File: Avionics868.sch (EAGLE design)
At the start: 65 parts, among them SW1 B3U-1000P-2P-SMD, U1 ATSAMD21G18_QFN, U2 SPX3819M5-L-3-0, U3 MCP73831T-2ACI/OT, U4 MPU-9250, U5 SIM868, U6 BMP180, X1 JSTPH, X2 32.768, X3 ST-USB-001G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

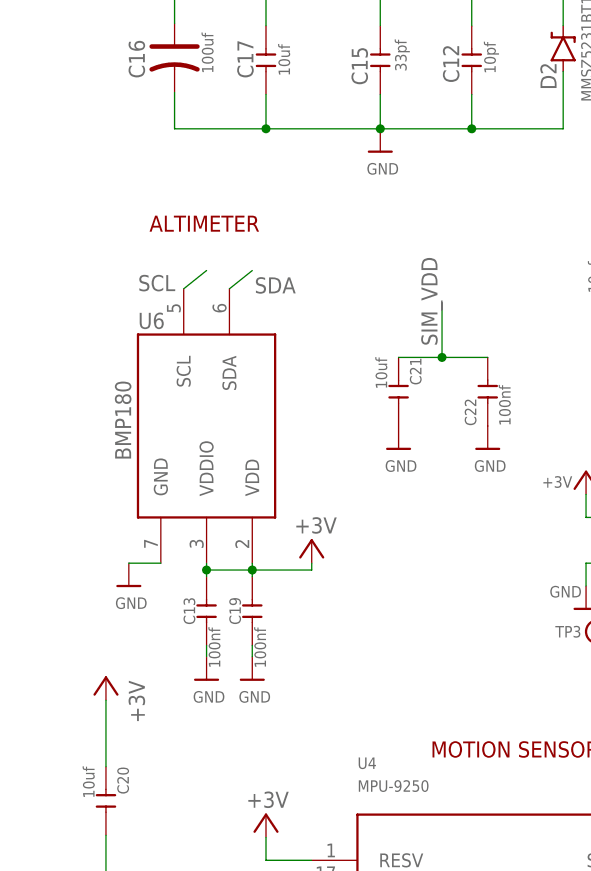
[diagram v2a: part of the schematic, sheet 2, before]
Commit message: Swapped obsolete part BMP180 for BMP280
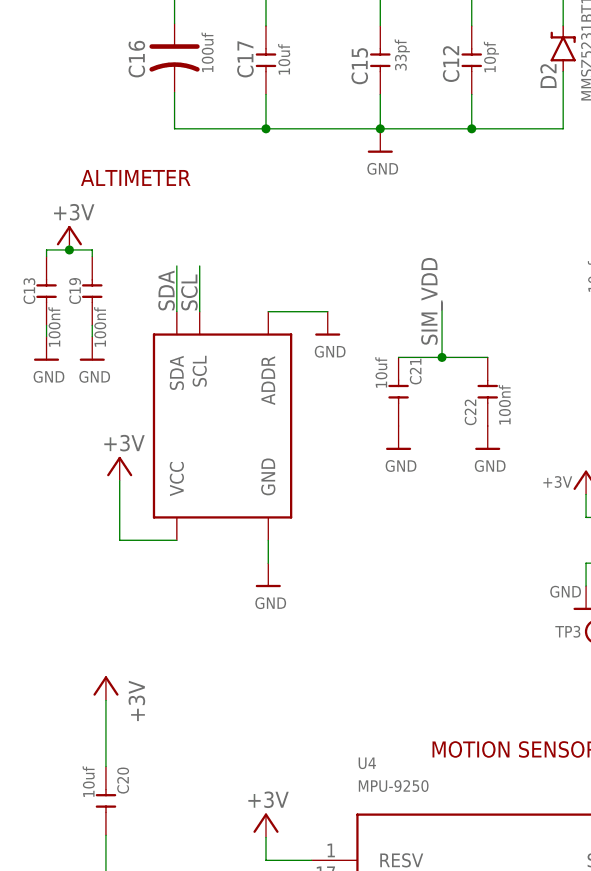
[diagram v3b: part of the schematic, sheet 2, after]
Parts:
- U6: value BMP180 -> BMP280; device SparkFun-Sensors:BMP180 -> BMP280:BMP280
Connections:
- net +3V: now also U6.VCC; no longer U6.VDD, U6.VDDIO
- net GND: now also U6.ADDR
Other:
- moved on the sheet: C13, C19
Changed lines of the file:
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@@
 <part name="R1" library="Seeed-Resistor-2016" deviceset="SMD-RES-100K-5%-1/10W(0603)" device="" value="100K 1/10W"/>
 <part name="FRAME2" library="microbuilder" deviceset="FRAME_A4" device=""/>
-<part name="U6" library="SparkFun-Sensors" deviceset="BMP180" device=""/>
 <part name="U4" library="misc" deviceset="MPU-9250" device=""/>
 <part name="C13" library="Seeed-Capacitor-2016" deviceset="CERAMIC-100NF-25V-10%-X7R(0402)" device="" value="100nf"/>
@@
 <part name="U$14" library="microbuilder" deviceset="GND" device=""/>
 <part name="U$15" library="microbuilder" deviceset="GND" device=""/>
-<part name="U$17" library="microbuilder" deviceset="GND" device=""/>
 <part name="U$18" library="microbuilder" deviceset="GND" device=""/>
 <part name="U$23" library="microbuilder" deviceset="GND" device=""/>
@@
 <part name="X3" library="Seeed-Connector -2016" deviceset="MICRO-USB-SMD-B-WITHOUT-POST-W/P(ST-USB-001G)" device="" value="ST-USB-001G"/>
 <part name="GND2" library="supply1" deviceset="GND" device=""/>
+<part name="U6" library="BMP280" deviceset="BMP280" device=""/>
+<part name="U$53" library="microbuilder" deviceset="GND" device=""/>
+<part name="U$54" library="microbuilder" deviceset="GND" device=""/>
+<part name="+3V15" library="Custom" deviceset="+3V" device=""/>
 </parts>
 <sheets>
@@
 <sheet>
 <plain>
-<text x="20.066" y="128.27" size="1.778" layer="94">ALTIMETER</text>
+<text x="12.446" y="133.35" size="1.778" layer="94">ALTIMETER</text>
 <text x="51.308" y="69.85" size="1.778" layer="94">MOTION SENSOR</text>
 <text x="91.44" y="129.54" size="1.778" layer="94">MICROSD / NANOSIM</text>
@@
 <instances>
 <instance part="FRAME2" gate="G$1" x="0" y="0"/>
-<instance part="U6" gate="G$1" x="26.416" y="106.68" smashed="yes" rot="R270">
-<attribute name="NAME" x="18.796" y="117.475" size="1.778" layer="95"/>
-<attribute name="VALUE" x="16.256" y="111.76" size="1.778" layer="96" rot="R270"/>
-</instance>
 <instance part="U4" gate="G$1" x="60.96" y="43.18"/>
-<instance part="C13" gate="G$1" x="26.416" y="86.106" smashed="yes" rot="R90">
-<attribute name="NAME" x="25.146" y="84.582" size="1.27" layer="95" ratio="10" rot="R90"/>
-<attribute name="VALUE" x="27.94" y="79.756" size="1.27" layer="96" ratio="10" rot="R90"/>
+<instance part="C13" gate="G$1" x="8.636" y="121.666" smashed="yes" rot="R90">
+<attribute name="NAME" x="7.366" y="120.142" size="1.27" layer="95" ratio="10" rot="R90"/>
+<attribute name="VALUE" x="10.16" y="115.316" size="1.27" layer="96" ratio="10" rot="R90"/>
 </instance>
 <instance part="C9" gate="G$1" x="97.79" y="30.48" rot="R180"/>
@@
 <instance part="U5" gate="G$1" x="198.12" y="68.58"/>
 <instance part="U$14" gate="G$1" x="45.72" y="137.16"/>
-<instance part="U$15" gate="G$1" x="26.416" y="78.486"/>
-<instance part="U$17" gate="G$1" x="17.78" y="88.9"/>
+<instance part="U$15" gate="G$1" x="8.636" y="114.046"/>
 <instance part="U$18" gate="G$1" x="104.14" y="27.94"/>
 <instance part="U$23" gate="G$1" x="88.9" y="40.64"/>
@@
 <instance part="U$26" gate="G$1" x="15.24" y="40.64"/>
 <instance part="U$37" gate="G$1" x="147.32" y="116.84"/>
-<instance part="+3V7" gate="G$1" x="38.1" y="93.98" smashed="yes" rot="MR0">
-<attribute name="VALUE" x="40.894" y="94.742" size="1.778" layer="96" rot="MR0"/>
+<instance part="+3V7" gate="G$1" x="11.176" y="128.778" smashed="yes" rot="MR0">
+<attribute name="VALUE" x="13.97" y="129.54" size="1.778" layer="96" rot="MR0"/>
 </instance>
 <instance part="+3V8" gate="G$1" x="91.44" y="55.88" smashed="yes" rot="MR0">
@@
 <attribute name="VALUE" x="33.274" y="49.276" size="1.778" layer="96" rot="MR0"/>
 </instance>
-<instance part="C19" gate="G$1" x="31.496" y="86.106" smashed="yes" rot="R90">
-<attribute name="NAME" x="30.226" y="84.582" size="1.27" layer="95" ratio="10" rot="R90"/>
-<attribute name="VALUE" x="33.02" y="79.756" size="1.27" layer="96" ratio="10" rot="R90"/>
-</instance>
-<instance part="U$7" gate="G$1" x="31.496" y="78.486"/>
+<instance part="C19" gate="G$1" x="13.716" y="121.666" smashed="yes" rot="R90">
+<attribute name="NAME" x="12.446" y="120.142" size="1.27" layer="95" ratio="10" rot="R90"/>
+<attribute name="VALUE" x="15.24" y="115.316" size="1.27" layer="96" ratio="10" rot="R90"/>
+</instance>
+<instance part="U$7" gate="G$1" x="13.716" y="114.046"/>
 <instance part="R4" gate="G$1" x="98.552" y="151.13" rot="R90"/>
 <instance part="R5" gate="G$1" x="106.172" y="151.13" rot="R90"/>
@@
 <instance part="U$35" gate="G$1" x="71.374" y="114.808"/>
 <instance part="U$51" gate="G$1" x="81.28" y="114.808"/>
+<instance part="U6" gate="G$1" x="28.194" y="106.68" rot="R90"/>
+<instance part="U$53" gate="G$1" x="39.878" y="116.84"/>
+<instance part="U$54" gate="G$1" x="33.274" y="88.9"/>
+<instance part="+3V15" gate="G$1" x="16.764" y="103.124" smashed="yes" rot="MR0">
+<attribute name="VALUE" x="19.558" y="103.886" size="1.778" layer="96" rot="MR0"/>
+</instance>
 </instances>
 <busses>
@@
 <net name="GND" class="0">
 <segment>
-<pinref part="U6" gate="G$1" pin="GND"/>
-<wire x1="17.78" y1="91.44" x2="21.336" y2="91.44" width="0.1524" layer="91"/>
-<pinref part="U$17" gate="G$1" pin="GND"/>
-</segment>
-<segment>
 <pinref part="U$15" gate="G$1" pin="GND"/>
 <pinref part="C13" gate="G$1" pin="1"/>
-<wire x1="26.416" y1="81.026" x2="26.416" y2="82.296" width="0.1524" layer="91"/>
+<wire x1="8.636" y1="116.586" x2="8.636" y2="117.856" width="0.1524" layer="91"/>
 </segment>
 <segment>
@@
 <pinref part="U$7" gate="G$1" pin="GND"/>
 <pinref part="C19" gate="G$1" pin="1"/>
-<wire x1="31.496" y1="81.026" x2="31.496" y2="82.296" width="0.1524" layer="91"/>
+<wire x1="13.716" y1="116.586" x2="13.716" y2="117.856" width="0.1524" layer="91"/>
 </segment>
 <segment>
@@
 <pinref part="U$51" gate="G$1" pin="GND"/>
 </segment>
+<segment>
+<pinref part="U6" gate="G$1" pin="ADDR"/>
+<wire x1="33.274" y1="119.38" x2="39.878" y2="119.38" width="0.1524" layer="91"/>
+<pinref part="U$53" gate="G$1" pin="GND"/>
+</segment>
+<segment>
+<pinref part="U6" gate="G$1" pin="GND"/>
+<pinref part="U$54" gate="G$1" pin="GND"/>
+<wire x1="33.274" y1="91.44" x2="33.274" y2="93.98" width="0.1524" layer="91"/>
+</segment>
 </net>
 <net name="SCL" class="0">
-<segment>
-<pinref part="U6" gate="G$1" pin="SCL"/>
-<wire x1="23.876" y1="121.92" x2="26.416" y2="123.952" width="0.1524" layer="91"/>
-<label x="18.796" y="121.666" size="1.778" layer="95"/>
-</segment>
 <segment>
 <pinref part="U4" gate="G$1" pin="SCL/SCLK"/>
@@
 <pinref part="R4" gate="G$1" pin="1"/>
 </segment>
+<segment>
+<pinref part="U6" gate="G$1" pin="SCL"/>
+<wire x1="25.654" y1="119.38" x2="25.654" y2="124.46" width="0.1524" layer="91"/>
+<label x="25.4" y="119.38" size="1.778" layer="95" rot="R90"/>
+</segment>
 </net>
 <net name="SDA" class="0">
-<segment>
-<pinref part="U6" gate="G$1" pin="SDA"/>
-<wire x1="28.956" y1="121.92" x2="31.496" y2="123.952" width="0.1524" layer="91"/>
-<label x="31.75" y="121.412" size="1.778" layer="95"/>
-</segment>
 <segment>
 <pinref part="U4" gate="G$1" pin="SDA/SDI"/>
@@
 <label x="103.632" y="143.51" size="1.778" layer="95"/>
 <pinref part="R5" gate="G$1" pin="1"/>
+</segment>
+<segment>
+<pinref part="U6" gate="G$1" pin="SDA"/>
+<wire x1="23.114" y1="119.38" x2="23.114" y2="124.46" width="0.1524" layer="91"/>
+<label x="22.86" y="119.38" size="1.778" layer="95" rot="R90"/>
 </segment>
 </net>
@@
 <segment>
 <pinref part="C13" gate="G$1" pin="2"/>
-<wire x1="26.416" y1="91.44" x2="26.416" y2="90.678" width="0.1524" layer="91"/>
 <pinref part="C19" gate="G$1" pin="2"/>
-<wire x1="26.416" y1="90.678" x2="26.416" y2="89.916" width="0.1524" layer="91"/>
-<wire x1="31.496" y1="91.44" x2="31.496" y2="90.678" width="0.1524" layer="91"/>
-<wire x1="31.496" y1="90.678" x2="31.496" y2="89.916" width="0.1524" layer="91"/>
-<wire x1="26.416" y1="90.678" x2="31.496" y2="90.678" width="0.1524" layer="91"/>
+<wire x1="8.636" y1="126.238" x2="8.636" y2="125.476" width="0.1524" layer="91"/>
+<wire x1="13.716" y1="126.238" x2="13.716" y2="125.476" width="0.1524" layer="91"/>
+<wire x1="8.636" y1="126.238" x2="11.176" y2="126.238" width="0.1524" layer="91"/>
 <pinref part="+3V7" gate="G$1" pin="+3V"/>
-<wire x1="31.496" y1="90.678" x2="38.1" y2="90.678" width="0.1524" layer="91"/>
-<wire x1="38.1" y1="90.678" x2="38.1" y2="91.44" width="0.1524" layer="91"/>
-<junction x="26.416" y="90.678"/>
-<junction x="31.496" y="90.678"/>
-<pinref part="U6" gate="G$1" pin="VDD"/>
-<pinref part="U6" gate="G$1" pin="VDDIO"/>
+<wire x1="11.176" y1="126.238" x2="13.716" y2="126.238" width="0.1524" layer="91"/>
+<junction x="11.176" y="126.238"/>
 </segment>
 <segment>
@@
 <junction x="76.2" y="124.968"/>
 </segment>
-</net>
+<segment>
+<pinref part="U6" gate="G$1" pin="VCC"/>
+<wire x1="23.114" y1="93.98" x2="16.764" y2="93.98" width="0.1524" layer="91"/>
+<wire x1="16.764" y1="93.98" x2="16.764" y2="100.584" width="0.1524" layer="91"/>
+<pinref part="+3V15" gate="G$1" pin="+3V"/>
+</segment>
+</net>

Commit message: Made lots of tweaks!
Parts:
- removed GPS_ANT, GSM_ANT: U-FL, Seeed-Connector -2016:ANTENNA-CONN-U-FL(3P)
- added C25: 100nf, Seeed-Capacitor-2016:CERAMIC-100NF-50V-10%-X7R(0603)
- added C26: 10nf, Seeed-Capacitor-2016:CERAMIC-10NF-50V-10%-X7R(0603)
- added C27, C28, C29: 10uf, Seeed-Capacitor-2016:CERAMIC-10UF-10V-10%-X5R(0603)
- added X5, X6: U-FL, Seeed-Connector -2016:ANTENNA-CONN-U-FL(3P)
- C1, C14, C7: value 1uF -> 1uf; device microbuilder:CAP_CERAMIC0603_NO -> Seeed-Capacitor-2016:CERAMIC-1UF-25V-10%-X7R(0603)
- C10: device Seeed-Capacitor-2016:CERAMIC-10NF-50V-10%-X7R(0402) -> Seeed-Capacitor-2016:CERAMIC-10NF-50V-10%-X7R(0603)
- C11, C13, C9: device Seeed-Capacitor-2016:CERAMIC-100NF-25V-10%-X7R(0402) -> Seeed-Capacitor-2016:CERAMIC-100NF-50V-10%-X7R(0603)
- C12: device Seeed-Capacitor-2016:CERAMIC-10PF-50V-5%-NPO(0402) -> Seeed-Capacitor-2016:CERAMIC-10PF-50V-5%-NPO(0603)
- C15: device Seeed-Capacitor-2016:CERAMIC-33PF-50V-5%-NPO(0402) -> Custom:CERAMIC-33PF-50V-5%-NPO(0603)
- C19, C22, C24: value 100nf -> 10nf; device Seeed-Capacitor-2016:CERAMIC-100NF-25V-10%-X7R(0402) -> Seeed-Capacitor-2016:CERAMIC-10NF-50V-10%-X7R(0603)
- C2, C4: value 22pF -> 22pf; device microbuilder:CAP_CERAMIC0603_NO -> Seeed-Capacitor-2016:CERAMIC-22PF-50V-5%-NPO(0603)
- C21, C23: value 10uf -> 100nf; device Seeed-Capacitor-2016:CERAMIC-10UF-10V-10%-X5R(0603) -> Seeed-Capacitor-2016:CERAMIC-100NF-50V-10%-X7R(0603)
- R3, R9: device Seeed-Resistor-2016:SMD-RES-100K-1%-1/16W(0402) -> Seeed-Resistor-2016:SMD-RES-100K-1%-1/10W(0603)
- R4, R5: device Seeed-Resistor-2016:SMD-RES-4.7K-5%-1/16W(0402) -> Seeed-Resistor-2016:SMD-RES-4.7K-5%-1/10W(0603)
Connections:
- net +3V: now also C20.2, C23.2, C27.2, C28.2; no longer C20.1, C23.1
- net GND: now also C20.1, C21.1, C23.1, C25.1, C26.1, C27.1, C28.1, C29.1, X5.GND1, X5.GND2, X6.GND1, X6.GND2; no longer C20.2, C21.2, C23.2, GPS_ANT.GND1, GPS_ANT.GND2, GSM_ANT.GND1, GSM_ANT.GND2
- net GPS_ANT: now also X6.D; no longer GPS_ANT.D
- net GSM_ANT: now also X5.D; no longer GSM_ANT.D
- net SIM_VDD: now also C21.2, C29.2; no longer C21.1
- net VBAT: now also C25.2, C26.2
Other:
- note added: "ANTENNAS"
- note added: "ESD SIM-CARD"
- note added: "SIM+SD COMBO SLOT"
- note removed: "ESD-PROTECTION"
- note removed: "GPS+GSM DECOUPLING"
- note removed: "MICROSD / NANOSIM"
- moved on the sheet: C10, C11, C12, C13, C15, C16, C17, C18, C19, C20, C21, C22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

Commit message: LOTS of tweaks. No more 403s.
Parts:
- removed C27: 10uf, Seeed-Capacitor-2016:CERAMIC-10UF-10V-10%-X5R(0603)
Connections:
- net +3V: no longer C27.2
- net GND: no longer C27.1
- net SIM_CLK: now also D3.C1; no longer D3.C3
- net SIM_DATA: now also D3.C2; no longer D3.C4
- net SIM_RST: now also D3.C4; no longer D3.C2
- net SIM_VDD: now also D3.C3; no longer D3.C1
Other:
- moved on the sheet: C13, C19, C20

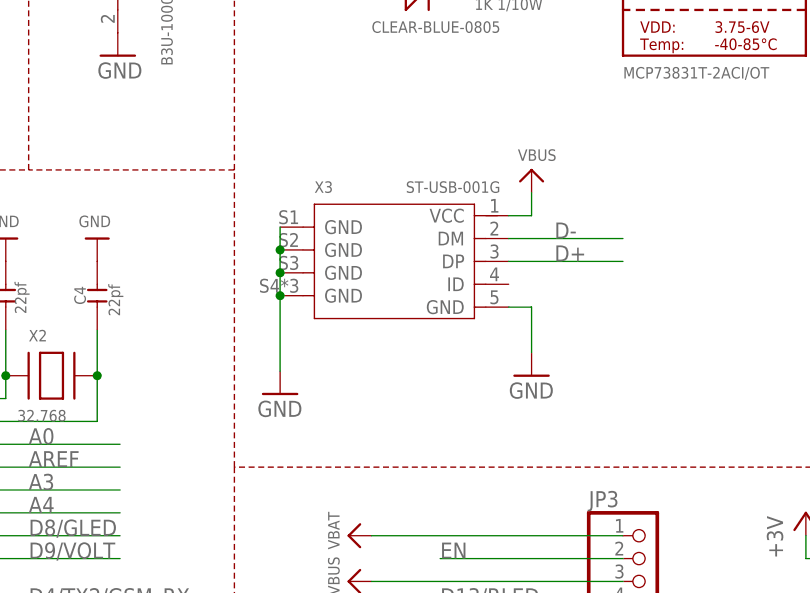
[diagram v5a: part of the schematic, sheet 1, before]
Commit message: Swapped USB port to deegou
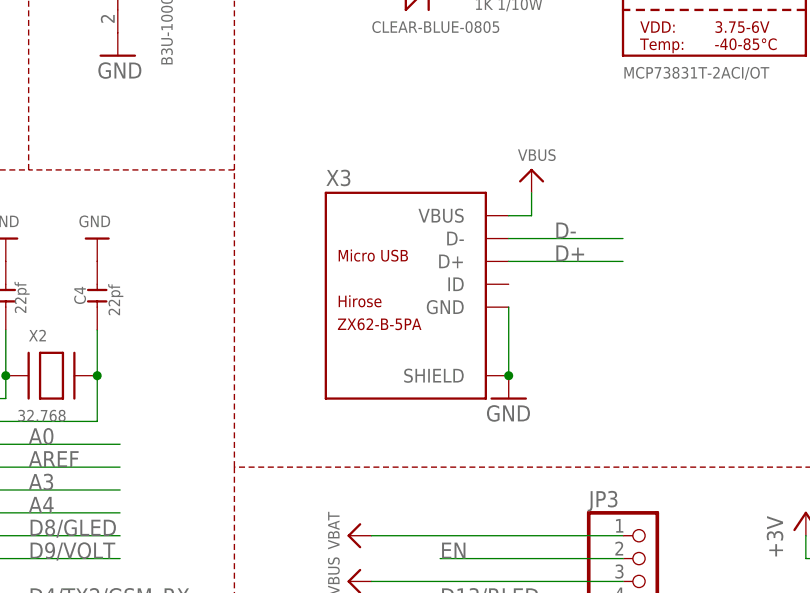
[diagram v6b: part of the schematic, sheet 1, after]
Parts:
- X3: value ST-USB-001G -> (none); device Seeed-Connector -2016:MICRO-USB-SMD-B-WITHOUT-POST-W/P(ST-USB-001G) -> Deegou-Connectors:AO1SB141B1-067
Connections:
- net D+: now also X3.D+; no longer X3.DP
- net D-: now also X3.D-; no longer X3.DM
- net GND: now also X3.GND, X3.SHIELD; no longer X3.GND@1, X3.GND@2, X3.GND@3, X3.GND@4, X3.GND@5
- net VBUS: now also X3.VBUS; no longer X3.VCC
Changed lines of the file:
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@@
 <part name="U$45" library="microbuilder" deviceset="GND" device=""/>
 <part name="SW1" library="Seeed-Switch-2016" deviceset="SMD-BUTTON(2P-3.0X2.5X1.2+0.4MM)" device="-B3U-1000P-2P-SMD" value="B3U-1000P-2P-SMD"/>
-<part name="X3" library="Seeed-Connector -2016" deviceset="MICRO-USB-SMD-B-WITHOUT-POST-W/P(ST-USB-001G)" device="" value="ST-USB-001G"/>
-<part name="GND2" library="supply1" deviceset="GND" device=""/>
 <part name="U6" library="BMP280" deviceset="BMP280" device=""/>
 <part name="U$53" library="microbuilder" deviceset="GND" device=""/>
@@
 <part name="U$13" library="microbuilder" deviceset="VBAT" device=""/>
 <part name="U$14" library="microbuilder" deviceset="GND" device=""/>
+<part name="X3" library="Deegou-Connectors" deviceset="AO1SB141B1-067" device=""/>
 </parts>
 <sheets>
@@
 <instance part="U$29" gate="G$1" x="50.8" y="127"/>
 <instance part="U$30" gate="G$1" x="27.94" y="127"/>
-<instance part="GND1" gate="1" x="167.64" y="99.06"/>
+<instance part="GND1" gate="1" x="165.1" y="96.52"/>
 <instance part="GND12" gate="1" x="83.82" y="127" rot="MR0"/>
 <instance part="L1" gate="G$1" x="246.38" y="50.8" rot="R270"/>
@@
 <attribute name="VALUE" x="126.492" y="148.844" size="1.27" layer="96" ratio="10" rot="R270"/>
 </instance>
-<instance part="X3" gate="USB" x="152.4" y="111.76"/>
-<instance part="GND2" gate="1" x="139.7" y="97.028"/>
+<instance part="X3" gate="G$1" x="154.94" y="106.68"/>
 </instances>
 <busses>
@@
 <pinref part="U$29" gate="G$1" pin="GND"/>
 <wire x1="50.8" y1="130.81" x2="50.8" y2="129.54" width="0.1524" layer="91"/>
-</segment>
-<segment>
-<wire x1="165.1" y1="106.68" x2="167.64" y2="106.68" width="0.1524" layer="91"/>
-<wire x1="167.64" y1="106.68" x2="167.64" y2="101.6" width="0.1524" layer="91"/>
-<pinref part="GND1" gate="1" pin="GND"/>
-<pinref part="X3" gate="USB" pin="GND@5"/>
 </segment>
 <segment>
@@
 </segment>
 <segment>
-<pinref part="X3" gate="USB" pin="GND@1"/>
-<wire x1="139.7" y1="115.57" x2="139.7" y2="113.03" width="0.1524" layer="91"/>
-<pinref part="GND2" gate="1" pin="GND"/>
-<pinref part="X3" gate="USB" pin="GND@2"/>
-<junction x="139.7" y="113.03"/>
-<wire x1="139.7" y1="113.03" x2="139.7" y2="110.49" width="0.1524" layer="91"/>
-<pinref part="X3" gate="USB" pin="GND@3"/>
-<junction x="139.7" y="110.49"/>
-<wire x1="139.7" y1="110.49" x2="139.7" y2="107.95" width="0.1524" layer="91"/>
-<pinref part="X3" gate="USB" pin="GND@4"/>
-<junction x="139.7" y="107.95"/>
-<wire x1="139.7" y1="107.95" x2="139.7" y2="99.568" width="0.1524" layer="91"/>
+<wire x1="165.1" y1="106.68" x2="165.1" y2="99.06" width="0.1524" layer="91"/>
+<pinref part="GND1" gate="1" pin="GND"/>
+<pinref part="X3" gate="G$1" pin="GND"/>
+<pinref part="X3" gate="G$1" pin="SHIELD"/>
+<junction x="165.1" y="99.06"/>
 </segment>
 </net>
@@
 <wire x1="167.64" y1="116.84" x2="167.64" y2="119.38" width="0.1524" layer="91"/>
 <pinref part="U$1" gate="G$1" pin="VBUS"/>
-<pinref part="X3" gate="USB" pin="VCC"/>
+<pinref part="X3" gate="G$1" pin="VBUS"/>
 </segment>
 <segment>
@@
 <wire x1="165.1" y1="111.76" x2="177.8" y2="111.76" width="0.1524" layer="91"/>
 <label x="170.18" y="111.76" size="1.778" layer="95"/>
-<pinref part="X3" gate="USB" pin="DP"/>
+<pinref part="X3" gate="G$1" pin="D+"/>
 </segment>
 <segment>
@@
 <wire x1="177.8" y1="114.3" x2="165.1" y2="114.3" width="0.1524" layer="91"/>
 <label x="170.18" y="114.3" size="1.778" layer="95"/>
-<pinref part="X3" gate="USB" pin="DM"/>
-</segment>
-<segment>
+<pinref part="X3" gate="G$1" pin="D-"/>
+</segment>
+<segment>

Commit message: added seeed MPN as attribute on Deegou USB port
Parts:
- X3: value (none) -> ZX62-B-5PA; SEEED (none) -> ZX62-B-5PA
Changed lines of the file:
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@@
 <part name="U$13" library="microbuilder" deviceset="VBAT" device=""/>
 <part name="U$14" library="microbuilder" deviceset="GND" device=""/>
-<part name="X3" library="Deegou-Connectors" deviceset="AO1SB141B1-067" device=""/>
+<part name="X3" library="Deegou-Connectors" deviceset="AO1SB141B1-067" device="" value="ZX62-B-5PA">
+<attribute name="SEEED" value="ZX62-B-5PA"/>
+</part>
 </parts>
 <sheets>
@@
 <attribute name="VALUE" x="126.492" y="148.844" size="1.27" layer="96" ratio="10" rot="R270"/>
 </instance>
-<instance part="X3" gate="G$1" x="154.94" y="106.68"/>
+<instance part="X3" gate="G$1" x="154.94" y="106.68">
+<attribute name="SEEED" x="154.94" y="106.68" size="1.778" layer="96" display="off"/>
+</instance>
 </instances>
 <busses>
